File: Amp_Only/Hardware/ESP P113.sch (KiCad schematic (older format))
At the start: 47 parts, among them J1 L_In, J2 R_In, J3 L_Out, J4 R_Out, Q1 MJE15032, Q2 MJE15033, Q3 MJE15032, Q4 MJE15033, U1 LM4562

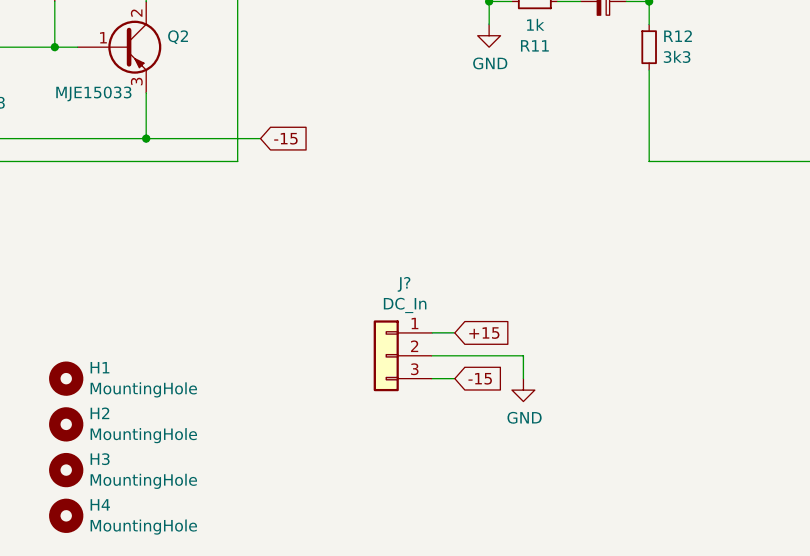
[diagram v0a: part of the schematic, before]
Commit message: Fixed amp only schematic
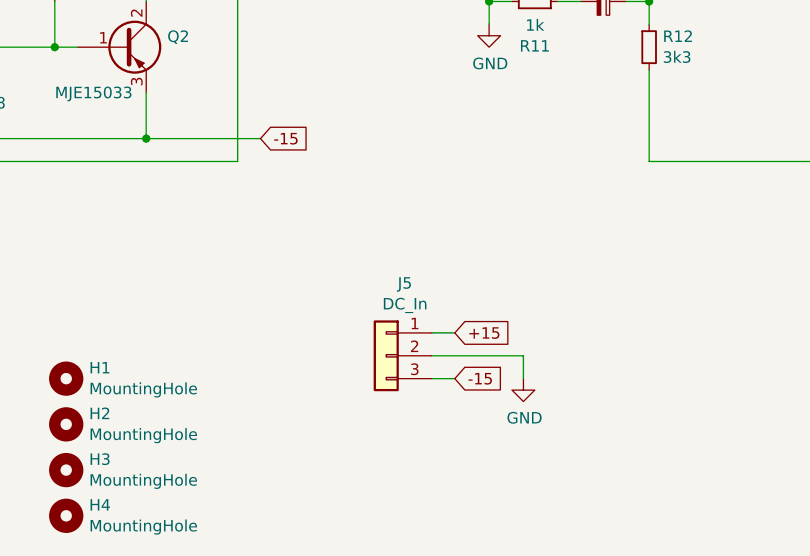
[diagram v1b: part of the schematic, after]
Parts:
- gave numbers to parts that had none: 1
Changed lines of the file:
@@
 $EndComp
 $Comp
-L Connector_Generic:Conn_01x03 J?
+L Connector_Generic:Conn_01x03 J5
 U 1 1 60B2DBBD
 P 4550 3500
-F 0 "J?" H 4468 3817 50  0000 C CNN
+F 0 "J5" H 4468 3817 50  0000 C CNN
 F 1 "DC_In" H 4468 3726 50  0000 C CNN
 F 2 "TerminalBlock_Phoenix:TerminalBlock_Phoenix_MKDS-1,5-3-5.08_1x03_P5.08mm_Horizontal" H 4550 3500 50  0001 C CNN
